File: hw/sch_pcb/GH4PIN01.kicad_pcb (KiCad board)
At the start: 2 copper layers, 40.1 x 40.1 mm, 7 parts, among them J1 SM04B-GHS-TB, J2 SM04B-GHS-TB, J3 HEADER_2x05_PARALLEL, M1 HOLE M3, M2 HOLE M3, M3 HOLE, M4 HOLE

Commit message: Cleanup and save in KiCAD 7.
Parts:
- J1, J2: moved to B.Cu
- moved J1 13.4 mm to (126.0, 104.1), turned to -90 degrees
- moved J2 11.5 mm to (126.0, 93.0), turned to -90 degrees
- moved J3 7.64 mm to (112.0, 96.5)

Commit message: The routed layout.
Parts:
- added J4: SM04B-GHS-TB, Connector_JST:JST_GH_SM04B-GHS-TB_1x04-1MP_P1.25mm_Horizontal, B.Cu at (141.3, 99.4)
- added J5: SM04B-GHS-TB, Connector_JST:JST_GH_SM04B-GHS-TB_1x04-1MP_P1.25mm_Horizontal, B.Cu at (141.3, 110.6)
- moved M2 42.7 mm to (153.6, 89.8)
- moved J3 37.5 mm to (148.5, 105.0)
- moved M3 32.8 mm to (143.4, 120.2)
- moved J1 30.4 mm to (155.7, 110.6)
- moved J2 30.4 mm to (155.7, 99.4)
- moved M4 14.2 mm to (153.6, 120.2)
- moved M1 8.56 mm to (143.4, 89.8)
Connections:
- net Net-(J2-Pad1) renamed /+5V
- net Net-(J3-Pad3) renamed /SCL
- net Net-(J3-Pad7) renamed /SDA
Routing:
- net /SDA: track 0.00 -> 40.9 mm, vias 0 -> 2
- net /+5V: track 0.00 -> 34.7 mm, vias 0 -> 3
- net /SCL: track 0.00 -> 34.2 mm
- net GND: track 0.00 -> 7.66 mm, vias 0 -> 2
- added copper zone on B.Cu, net GND
- added copper zone on F.Cu, net GND
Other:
- board size 40.1 x 40.1 mm -> 19.8 x 40.1 mm
- rule pad_to_mask_clearance: 0 -> 0.08
- board text added: "+5V"
- board text added: "GH4PIN01A"
- board text added: "GND"
- board text added: "MLAB.cz"
- board text added: "SCL"
- board text added: "SDA"
- board text added: "Vdd"

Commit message: Improve manufacturing texts.
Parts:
- added FID1: Fiducial, Fiducial:Fiducial_1mm_Mask2mm, B.Cu at (148.5, 87.1)
- added FID2: Fiducial, Fiducial:Fiducial_1mm_Mask2mm, B.Cu at (148.6, 123.1)
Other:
- board text added: "J4"
- board text added: "Kaklik 2024"
- board text removed: "Vdd"
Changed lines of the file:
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@@
     (property "Sheetname" "")
     (attr smd)
-    (fp_text reference "J1" (at 0 3.9 90) (layer "B.SilkS")
+    (fp_text reference "J1" (at 3.9116 2.5908 90) (layer "B.SilkS")
         (effects (font (size 1 1) (thickness 0.15)) (justify mirror))
     )
@@
     (property "Sheetname" "")
     (attr smd)
-    (fp_text reference "J5" (at 0 3.9 90) (layer "B.SilkS")
+    (fp_text reference "J5" (at -3.7592 2.6924 90) (layer "B.SilkS")
         (effects (font (size 1 1) (thickness 0.15)) (justify mirror))
     )
@@
     )
   )
+  (footprint "Fiducial:Fiducial_1mm_Mask2mm" (layer "B.Cu")
+    (at 148.550799 123.0848 180)
+    (descr "Circular Fiducial, 1mm bare copper, 2mm soldermask opening (Level A)")
+    (tags "fiducial")
+    (property "Sheetfile" "GH4PIN01.kicad_sch")
+    (property "Sheetname" "")
+    (property "ki_description" "Fiducial Marker")
+    (property "ki_keywords" "fiducial marker")
+    (attr smd)
+    (fp_text reference "FID2" (at 0 2) (layer "B.SilkS") hide
+        (effects (font (size 1 1) (thickness 0.15)) (justify mirror))
+    )
+    (fp_text value "Fiducial" (at 0 -2) (layer "B.Fab")
+        (effects (font (size 1 1) (thickness 0.15)) (justify mirror))
+    )
+    (fp_text user "${REFERENCE}" (at 0 0) (layer "B.Fab")
+        (effects (font (size 0.4 0.4) (thickness 0.06)) (justify mirror))
+    )
+    (fp_circle (center 0 0) (end 1.25 0)
+      (stroke (width 0.05) (type solid)) (fill none) (layer "B.CrtYd"))
+    (fp_circle (center 0 0) (end 1 0)
+      (stroke (width 0.1) (type solid)) (fill none) (layer "B.Fab"))
+    (pad "" smd circle (at 0 0 180) (size 1 1) (layers "B.Cu" "B.Mask")
+      (solder_mask_margin 0.5) (clearance 0.5))
+  )
+  (footprint "Fiducial:Fiducial_1mm_Mask2mm" (layer "B.Cu")
+    (at 148.499999 87.0736 180)
+    (descr "Circular Fiducial, 1mm bare copper, 2mm soldermask opening (Level A)")
+    (tags "fiducial")
+    (property "Sheetfile" "GH4PIN01.kicad_sch")
+    (property "Sheetname" "")
+    (property "ki_description" "Fiducial Marker")
+    (property "ki_keywords" "fiducial marker")
+    (attr smd)
+    (fp_text reference "FID1" (at 0 2) (layer "B.SilkS") hide
+        (effects (font (size 1 1) (thickness 0.15)) (justify mirror))
+    )
+    (fp_text value "Fiducial" (at 0 -2) (layer "B.Fab")
+        (effects (font (size 1 1) (thickness 0.15)) (justify mirror))
+    )
+    (fp_text user "${REFERENCE}" (at 0 0) (layer "B.Fab")
+        (effects (font (size 0.4 0.4) (thickness 0.06)) (justify mirror))
+    )
+    (fp_circle (center 0 0) (end 1.25 0)
+      (stroke (width 0.05) (type solid)) (fill none) (layer "B.CrtYd"))
+    (fp_circle (center 0 0) (end 1 0)
+      (stroke (width 0.1) (type solid)) (fill none) (layer "B.Fab"))
+    (pad "" smd circle (at 0 0 180) (size 1 1) (layers "B.Cu" "B.Mask")
+      (solder_mask_margin 0.5) (clearance 0.5))
+  )
   (footprint "Connector_JST:JST_GH_SM04B-GHS-TB_1x04-1MP_P1.25mm_Horizontal" (layer "B.Cu")
     (at 155.713599 99.3612 -90)
@@
     (property "Sheetname" "")
     (attr smd)
-    (fp_text reference "J2" (at 0 3.9 90) (layer "B.SilkS")
+    (fp_text reference "J2" (at 3.4036 2.8956 90) (layer "B.SilkS")
         (effects (font (size 1 1) (thickness 0.15)) (justify mirror))
     )
@@
     (property "Sheetname" "")
     (attr smd)
-    (fp_text reference "J4" (at 0 3.9 90) (layer "B.SilkS")
+    (fp_text reference "J4" (at -4.2672 2.6924 90) (layer "B.SilkS")
         (effects (font (size 1 1) (thickness 0.15)) (justify mirror))
     )
@@
         (effects (font (size 1 1) (thickness 0.15)) (justify mirror))
     )
-    (fp_text user "${REFERENCE}" (at 0 0 90) (layer "B.Fab")
+    (fp_text user "${REFERENCE}" (at 0 0.6858 90) (layer "B.Fab")
         (effects (font (size 1 1) (thickness 0.15)) (justify mirror))
     )
@@
   (gr_rect (start 138.594 84.934) (end 158.406 125.066)
     (stroke (width 0.15) (type default)) (fill none) (layer "Edge.Cuts"))
-  (gr_text "GND" (at 138.974999 98.015) (layer "F.SilkS")
-    (effects (font (size 0.8 1) (thickness 0.15)) (justify left bottom))
-  )
-  (gr_text "SCL" (at 138.974999 100.555) (layer "F.SilkS")
-    (effects (font (size 0.8 1) (thickness 0.15)) (justify left bottom))
-  )
-  (gr_text "+5V" (at 138.847999 101.825) (layer "F.SilkS")
+  (gr_text "MLAB.cz" (at 149.058799 92.6048 90) (layer "F.Cu")
+    (effects (font (size 1 1) (thickness 0.15)) (justify left bottom))
+  )
+  (gr_text "GH4PIN01A" (at 152.563999 96.11) (layer "B.Cu")
+    (effects (font (size 1 1) (thickness 0.15)) (justify left bottom mirror))
+  )
+  (gr_text "Kaklik\n2024" (at 148.499999 115.5156) (layer "B.Cu")
+    (effects (font (size 1 1) (thickness 0.15)) (justify bottom mirror))
+  )
+  (gr_text "GND" (at 139.660799 98.015) (layer "F.SilkS")
+    (effects (font (size 0.8 1) (thickness 0.15)) (justify left bottom))
+  )
+  (gr_text "SCL" (at 139.660799 100.555) (layer "F.SilkS")
+    (effects (font (size 0.8 1) (thickness 0.15)) (justify left bottom))
+  )
+  (gr_text "+5V" (at 139.533799 101.825) (layer "F.SilkS")
     (effects (font (size 0.8 1) (thickness 0.15)) (justify left bottom))
   )
@@
     (effects (font (size 1 1) (thickness 0.15)) (justify left bottom))
   )
-  (gr_text "SDA" (at 138.974999 99.285) (layer "F.SilkS")
-    (effects (font (size 0.8 1) (thickness 0.15)) (justify left bottom))
-  )
-  (gr_text "MLAB.cz" (at 145.324999 116.303) (layer "F.SilkS")
-    (effects (font (size 1 1) (thickness 0.15)) (justify left bottom))
+  (gr_text "SDA" (at 139.660799 99.285) (layer "F.SilkS")
+    (effects (font (size 0.8 1) (thickness 0.15)) (justify left bottom))
+  )
+  (gr_text "SCL" (at 139.432199 111.7564) (layer "F.SilkS")
+    (effects (font (size 0.8 1) (thickness 0.15)) (justify left bottom))
+  )
+  (gr_text "MLAB.cz" (at 149.261999 123.4404 90) (layer "F.SilkS")
+    (effects (font (size 1 1) (thickness 0.15)) (justify left bottom))
+  )
+  (gr_text "Kaklik\n2024" (at 148.550799 115.5156) (layer "F.SilkS")
+    (effects (font (size 1 1) (thickness 0.15)) (justify bottom))
+  )
+  (gr_text "SDA" (at 139.432199 110.4864) (layer "F.SilkS")
+    (effects (font (size 0.8 1) (thickness 0.15)) (justify left bottom))
+  )
+  (gr_text "+5V" (at 139.305199 113.0264) (layer "F.SilkS")
+    (effects (font (size 0.8 1) (thickness 0.15)) (justify left bottom))
   )
   (gr_text "GH4PIN01A" (at 144.181999 96.11) (layer "F.SilkS")
@@
     (effects (font (size 1 1) (thickness 0.15)) (justify left bottom))
   )
+  (gr_text "GND" (at 139.432199 109.2164) (layer "F.SilkS")
+    (effects (font (size 0.8 1) (thickness 0.15)) (justify left bottom))
+  )
   (gr_text "SDA" (at 151.420999 108.302) (layer "F.SilkS")
     (effects (font (size 1 1) (thickness 0.15)) (justify left bottom))
   )
-  (gr_text "Vdd" (at 151.420999 105.762) (layer "F.SilkS")
+  (gr_text "+5V" (at 151.420999 105.762) (layer "F.SilkS")
     (effects (font (size 1 1) (thickness 0.15)) (justify left bottom))
   )
@@
     (effects (font (size 1 1) (thickness 0.15)) (justify left bottom))
   )
+  (gr_text "J4" (at 141.743599 110.5626) (layer "B.Fab")
+    (effects (font (size 1 1) (thickness 0.15)) (justify mirror))
+  )
   (dimension (type aligned) (layer "Cmts.User")

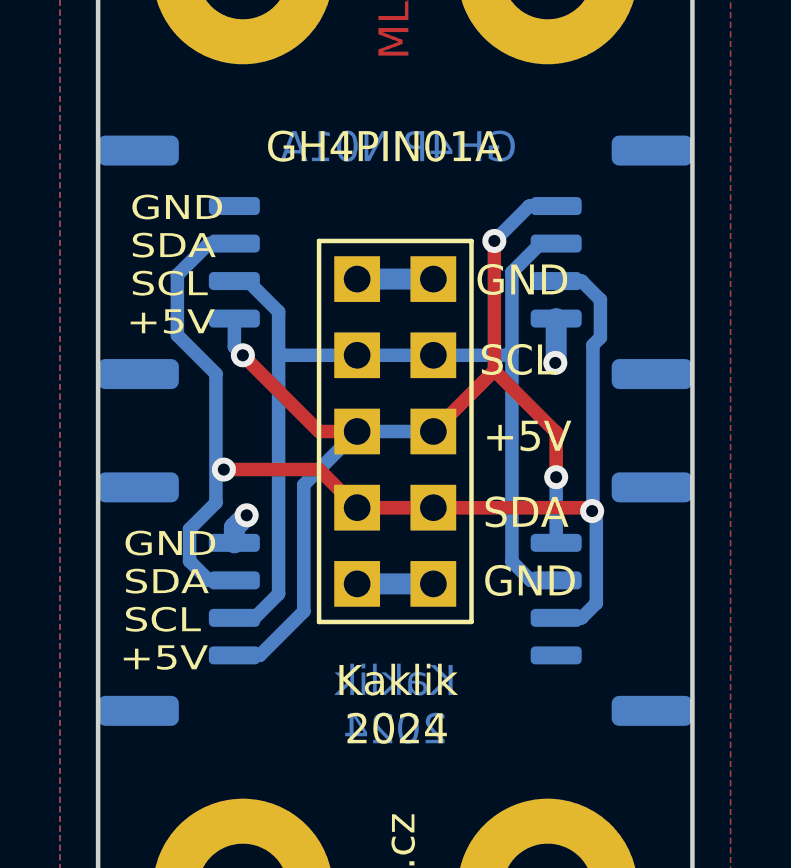
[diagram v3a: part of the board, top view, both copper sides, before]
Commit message: Add labels for CAN bus.
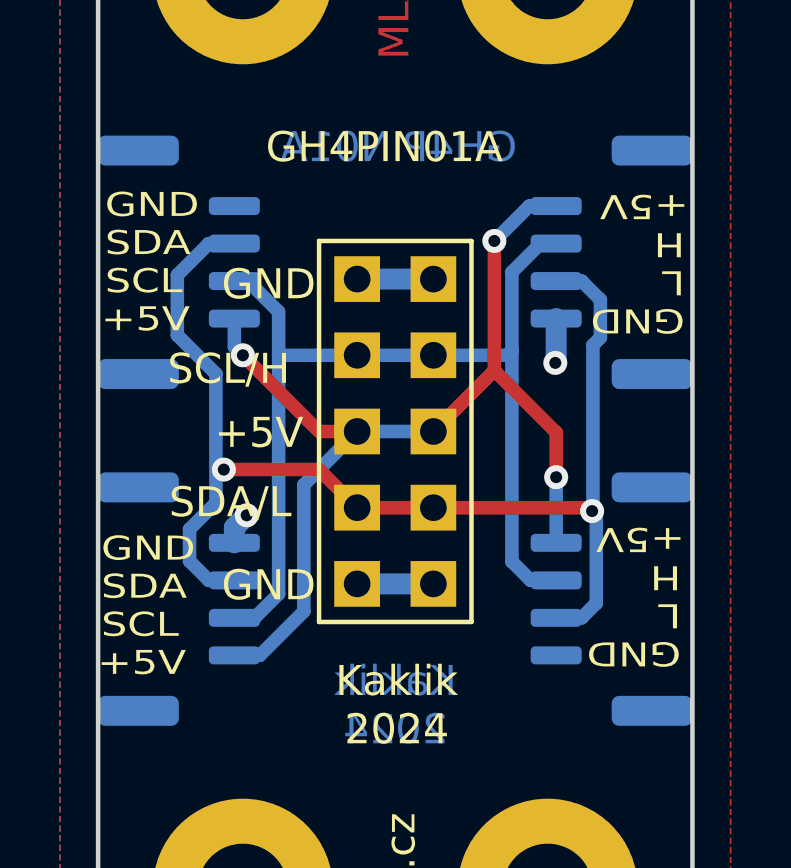
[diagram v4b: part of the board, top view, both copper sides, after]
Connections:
- net /SCL renamed /SCL/CAN_H
- net /SDA renamed /SDA/CAN_L
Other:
- board text added: "H"
- board text added: "L"
- board text added: "SCL/H"
- board text added: "SDA/L"
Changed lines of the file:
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@@
   (net 1 "/+5V")
   (net 2 "GND")
-  (net 3 "/SCL")
-  (net 4 "/SDA")
+  (net 3 "/SCL{slash}CAN_H")
+  (net 4 "/SDA{slash}CAN_L")
   (footprint "Mlab_Mechanical:MountingHole_3mm" locked placed (layer "F.Cu")
     (at 153.58 89.76)
@@
       (net 2 "GND") (pintype "input"))
     (pad "3" thru_hole rect (at -1.27 -2.54) (size 1.524 1.524) (drill 0.889) (layers "*.Cu" "*.Mask" "F.SilkS")
-      (net 3 "/SCL") (pintype "input"))
+      (net 3 "/SCL{slash}CAN_H") (pintype "input"))
     (pad "4" thru_hole rect (at 1.27 -2.54) (size 1.524 1.524) (drill 0.889) (layers "*.Cu" "*.Mask" "F.SilkS")
-      (net 3 "/SCL") (pintype "input"))
+      (net 3 "/SCL{slash}CAN_H") (pintype "input"))
     (pad "5" thru_hole rect (at -1.27 0) (size 1.524 1.524) (drill 0.889) (layers "*.Cu" "*.Mask" "F.SilkS")
       (net 1 "/+5V") (pintype "input"))
@@
       (net 1 "/+5V") (pintype "input"))
     (pad "7" thru_hole rect (at -1.27 2.54) (size 1.524 1.524) (drill 0.889) (layers "*.Cu" "*.Mask" "F.SilkS")
-      (net 4 "/SDA") (pintype "input"))
+      (net 4 "/SDA{slash}CAN_L") (pintype "input"))
     (pad "8" thru_hole rect (at 1.27 2.54) (size 1.524 1.524) (drill 0.889) (layers "*.Cu" "*.Mask" "F.SilkS")
-      (net 4 "/SDA") (pintype "input"))
+      (net 4 "/SDA{slash}CAN_L") (pintype "input"))
     (pad "9" thru_hole rect (at -1.27 5.08) (size 1.524 1.524) (drill 0.889) (layers "*.Cu" "*.Mask" "F.SilkS")
       (net 2 "GND") (pintype "input"))
@@
       (net 1 "/+5V") (pintype "input"))
     (pad "2" smd roundrect (at -0.625 1.85 270) (size 0.6 1.7) (layers "B.Cu" "B.Paste" "B.Mask") (roundrect_rratio 0.25)
-      (net 3 "/SCL") (pintype "input"))
+      (net 3 "/SCL{slash}CAN_H") (pintype "input"))
     (pad "3" smd roundrect (at 0.625 1.85 270) (size 0.6 1.7) (layers "B.Cu" "B.Paste" "B.Mask") (roundrect_rratio 0.25)
-      (net 4 "/SDA") (pintype "input"))
+      (net 4 "/SDA{slash}CAN_L") (pintype "input"))
     (pad "4" smd roundrect (at 1.875 1.85 270) (size 0.6 1.7) (layers "B.Cu" "B.Paste" "B.Mask") (roundrect_rratio 0.25)
       (net 2 "GND") (pintype "input"))
@@
       (net 1 "/+5V") (pintype "input"))
     (pad "2" smd roundrect (at -0.625 1.85 90) (size 0.6 1.7) (layers "B.Cu" "B.Paste" "B.Mask") (roundrect_rratio 0.25)
-      (net 3 "/SCL") (pintype "input"))
+      (net 3 "/SCL{slash}CAN_H") (pintype "input"))
     (pad "3" smd roundrect (at 0.625 1.85 90) (size 0.6 1.7) (layers "B.Cu" "B.Paste" "B.Mask") (roundrect_rratio 0.25)
-      (net 4 "/SDA") (pintype "input"))
+      (net 4 "/SDA{slash}CAN_L") (pintype "input"))
     (pad "4" smd roundrect (at 1.875 1.85 90) (size 0.6 1.7) (layers "B.Cu" "B.Paste" "B.Mask") (roundrect_rratio 0.25)
       (net 2 "GND") (pintype "input"))
@@
       (net 1 "/+5V") (pintype "input"))
     (pad "2" smd roundrect (at -0.625 1.85 270) (size 0.6 1.7) (layers "B.Cu" "B.Paste" "B.Mask") (roundrect_rratio 0.25)
-      (net 3 "/SCL") (pintype "input"))
+      (net 3 "/SCL{slash}CAN_H") (pintype "input"))
     (pad "3" smd roundrect (at 0.625 1.85 270) (size 0.6 1.7) (layers "B.Cu" "B.Paste" "B.Mask") (roundrect_rratio 0.25)
-      (net 4 "/SDA") (pintype "input"))
+      (net 4 "/SDA{slash}CAN_L") (pintype "input"))
     (pad "4" smd roundrect (at 1.875 1.85 270) (size 0.6 1.7) (layers "B.Cu" "B.Paste" "B.Mask") (roundrect_rratio 0.25)
       (net 2 "GND") (pintype "input"))
@@
       (net 1 "/+5V") (pintype "input"))
     (pad "2" smd roundrect (at -0.625 1.85 90) (size 0.6 1.7) (layers "B.Cu" "B.Paste" "B.Mask") (roundrect_rratio 0.25)
-      (net 3 "/SCL") (pintype "input"))
+      (net 3 "/SCL{slash}CAN_H") (pintype "input"))
     (pad "3" smd roundrect (at 0.625 1.85 90) (size 0.6 1.7) (layers "B.Cu" "B.Paste" "B.Mask") (roundrect_rratio 0.25)
-      (net 4 "/SDA") (pintype "input"))
+      (net 4 "/SDA{slash}CAN_L") (pintype "input"))
     (pad "4" smd roundrect (at 1.875 1.85 90) (size 0.6 1.7) (layers "B.Cu" "B.Paste" "B.Mask") (roundrect_rratio 0.25)
       (net 2 "GND") (pintype "input"))
@@
     (effects (font (size 1 1) (thickness 0.15)) (justify bottom mirror))
   )
-  (gr_text "GND" (at 139.660799 98.015) (layer "F.SilkS")
-    (effects (font (size 0.8 1) (thickness 0.15)) (justify left bottom))
-  )
-  (gr_text "SCL" (at 139.660799 100.555) (layer "F.SilkS")
-    (effects (font (size 0.8 1) (thickness 0.15)) (justify left bottom))
-  )
-  (gr_text "+5V" (at 139.533799 101.825) (layer "F.SilkS")
-    (effects (font (size 0.8 1) (thickness 0.15)) (justify left bottom))
-  )
-  (gr_text "GND" (at 151.166999 100.555) (layer "F.SilkS")
-    (effects (font (size 1 1) (thickness 0.15)) (justify left bottom))
-  )
-  (gr_text "SDA" (at 139.660799 99.285) (layer "F.SilkS")
-    (effects (font (size 0.8 1) (thickness 0.15)) (justify left bottom))
-  )
-  (gr_text "SCL" (at 139.432199 111.7564) (layer "F.SilkS")
+  (gr_text "+5V" (at 158.278999 97.0244 180) (layer "F.SilkS")
+    (effects (font (size 0.8 1) (thickness 0.15)) (justify left bottom))
+  )
+  (gr_text "GND" (at 138.822599 97.9134) (layer "F.SilkS")
+    (effects (font (size 0.8 1) (thickness 0.15)) (justify left bottom))
+  )
+  (gr_text "SCL" (at 138.822599 100.4534) (layer "F.SilkS")
+    (effects (font (size 0.8 1) (thickness 0.15)) (justify left bottom))
+  )
+  (gr_text "+5V" (at 138.695599 101.7234) (layer "F.SilkS")
+    (effects (font (size 0.8 1) (thickness 0.15)) (justify left bottom))
+  )
+  (gr_text "L" (at 158.151999 99.564401 180) (layer "F.SilkS")
+    (effects (font (size 0.8 1) (thickness 0.15)) (justify left bottom))
+  )
+  (gr_text "H" (at 158.024999 109.3942 180) (layer "F.SilkS")
+    (effects (font (size 0.8 1) (thickness 0.15)) (justify left bottom))
+  )
+  (gr_text "GND" (at 142.708799 110.715) (layer "F.SilkS")
+    (effects (font (size 1 1) (thickness 0.15)) (justify left bottom))
+  )
+  (gr_text "+5V" (at 158.151999 108.1242 180) (layer "F.SilkS")
+    (effects (font (size 0.8 1) (thickness 0.15)) (justify left bottom))
+  )
+  (gr_text "SDA" (at 138.822599 99.1834) (layer "F.SilkS")
+    (effects (font (size 0.8 1) (thickness 0.15)) (justify left bottom))
+  )
+  (gr_text "SCL" (at 138.695599 111.9088) (layer "F.SilkS")
+    (effects (font (size 0.8 1) (thickness 0.15)) (justify left bottom))
+  )
+  (gr_text "GND" (at 158.024999 111.9342 180) (layer "F.SilkS")
     (effects (font (size 0.8 1) (thickness 0.15)) (justify left bottom))
   )
@@
     (effects (font (size 1 1) (thickness 0.15)) (justify bottom))
   )
-  (gr_text "SDA" (at 139.432199 110.4864) (layer "F.SilkS")
-    (effects (font (size 0.8 1) (thickness 0.15)) (justify left bottom))
-  )
-  (gr_text "+5V" (at 139.305199 113.0264) (layer "F.SilkS")
+  (gr_text "SDA" (at 138.695599 110.6388) (layer "F.SilkS")
+    (effects (font (size 0.8 1) (thickness 0.15)) (justify left bottom))
+  )
+  (gr_text "+5V" (at 138.568599 113.1788) (layer "F.SilkS")
+    (effects (font (size 0.8 1) (thickness 0.15)) (justify left bottom))
+  )
+  (gr_text "GND" (at 142.708799 100.682) (layer "F.SilkS")
+    (effects (font (size 1 1) (thickness 0.15)) (justify left bottom))
+  )
+  (gr_text "+5V" (at 142.480199 105.635) (layer "F.SilkS")
+    (effects (font (size 1 1) (thickness 0.15)) (justify left bottom))
+  )
+  (gr_text "GND" (at 158.151999 100.8344 180) (layer "F.SilkS")
     (effects (font (size 0.8 1) (thickness 0.15)) (justify left bottom))
   )
@@
     (effects (font (size 1 1) (thickness 0.15)) (justify left bottom))
   )
-  (gr_text "SCL" (at 151.293999 103.222) (layer "F.SilkS")
-    (effects (font (size 1 1) (thickness 0.15)) (justify left bottom))
-  )
-  (gr_text "GND" (at 139.432199 109.2164) (layer "F.SilkS")
-    (effects (font (size 0.8 1) (thickness 0.15)) (justify left bottom))
-  )
-  (gr_text "SDA" (at 151.420999 108.302) (layer "F.SilkS")
-    (effects (font (size 1 1) (thickness 0.15)) (justify left bottom))
-  )
-  (gr_text "+5V" (at 151.420999 105.762) (layer "F.SilkS")
-    (effects (font (size 1 1) (thickness 0.15)) (justify left bottom))
-  )
-  (gr_text "GND" (at 151.420999 110.588) (layer "F.SilkS")
-    (effects (font (size 1 1) (thickness 0.15)) (justify left bottom))
-  )
+  (gr_text "L" (at 158.024999 110.664201 180) (layer "F.SilkS")
+    (effects (font (size 0.8 1) (thickness 0.15)) (justify left bottom))
+  )
+  (gr_text "GND" (at 138.695599 109.3688) (layer "F.SilkS")
+    (effects (font (size 0.8 1) (thickness 0.15)) (justify left bottom))
+  )
+  (gr_text "H" (at 158.151999 98.2944 180) (layer "F.SilkS")
+    (effects (font (size 0.8 1) (thickness 0.15)) (justify left bottom))
+  )
+  (gr_text "SDA/L" (at 140.956199 107.9464) (layer "F.SilkS")
+    (effects (font (size 1 1) (thickness 0.15)) (justify left bottom))
+  )
+  (gr_text "SCL/H" (at 140.905399 103.5014) (layer "F.SilkS")
+    (effects (font (size 1 1) (thickness 0.15)) (justify left bottom))
+  )
